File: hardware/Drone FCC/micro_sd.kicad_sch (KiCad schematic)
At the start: 15 parts, among them J701 DM3AT-SF-PEJM5

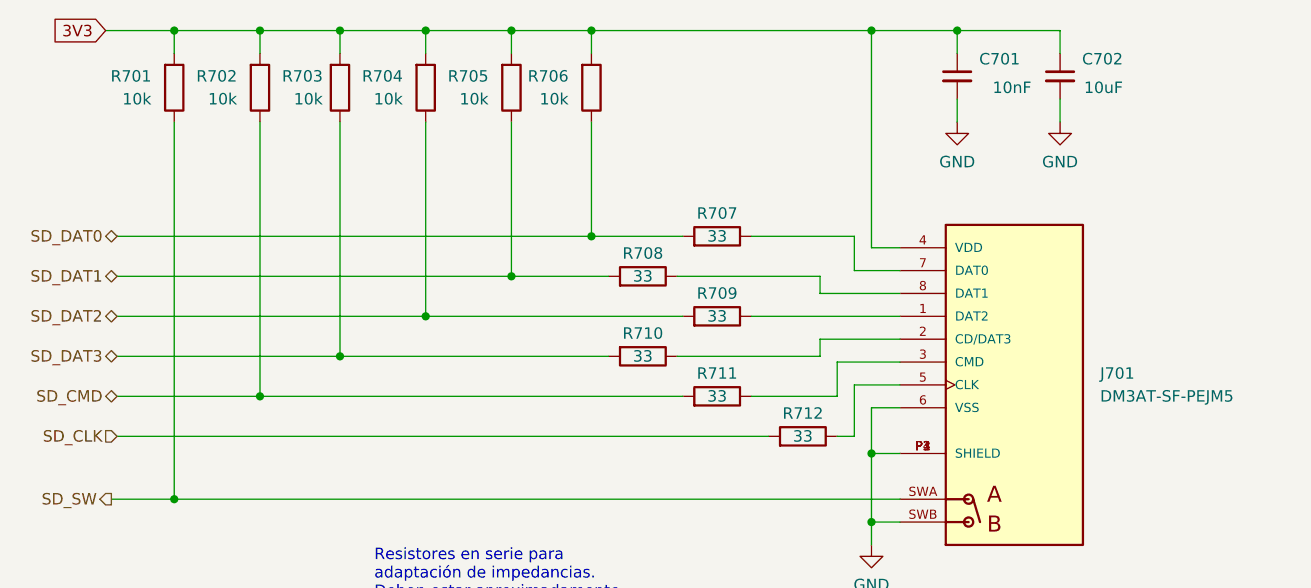
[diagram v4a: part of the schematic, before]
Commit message: re enumeation of componentes
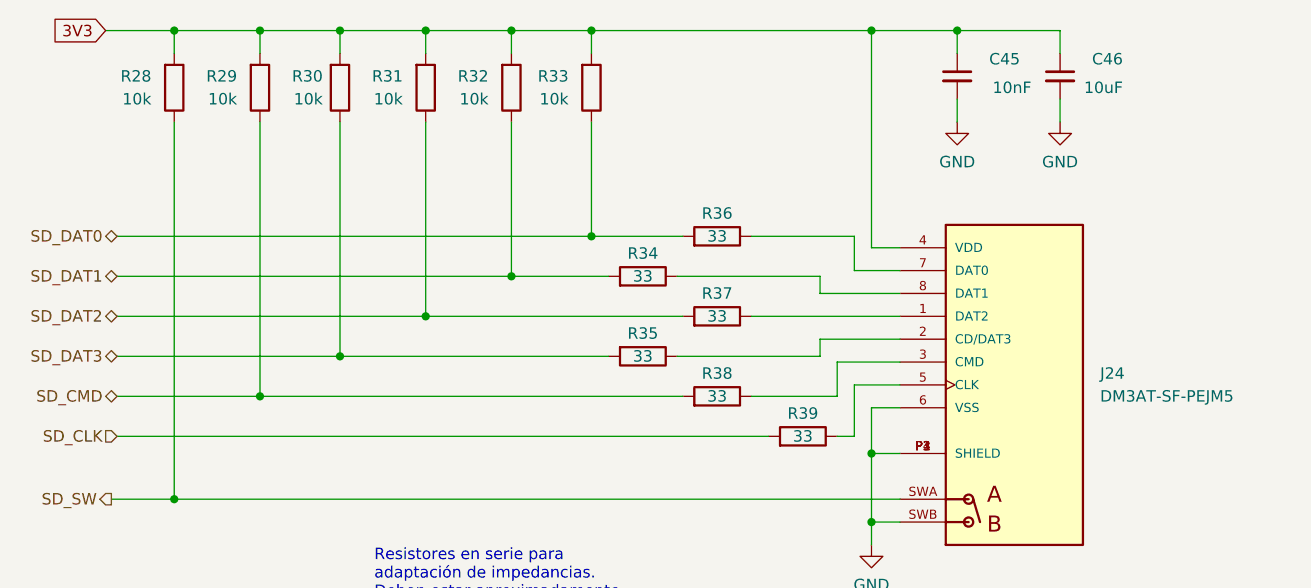
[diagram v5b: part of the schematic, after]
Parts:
- renumbered C701 to C45, C702 to C46, J701 to J24, R701 to R28, R702 to R29, R703 to R30, R704 to R31, R705 to R32, R706 to R33, R708 to R34, R710 to R35, R707 to R36, R709 to R37, R711 to R38, R712 to R39
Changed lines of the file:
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@@
   (symbol (lib_id "power:GND") (at 155.575 129.54 0) (unit 1)
     (in_bom yes) (on_board yes) (fields_autoplaced)
-    (property "Reference" "#PWR0144" (id 0) (at 155.575 135.89 0)
+    (property "Reference" "#PWR055" (id 0) (at 155.575 135.89 0)
       (effects (font (size 1.27 1.27)) hide)
     )
@@
   (symbol (lib_id "power:GND") (at 165.1 82.55 0) (unit 1)
     (in_bom yes) (on_board yes) (fields_autoplaced)
-    (property "Reference" "#PWR0142" (id 0) (at 165.1 88.9 0)
+    (property "Reference" "#PWR056" (id 0) (at 165.1 88.9 0)
       (effects (font (size 1.27 1.27)) hide)
     )
@@
   (symbol (lib_id "Device:R") (at 138.43 95.25 270) (mirror x) (unit 1)
     (in_bom yes) (on_board yes)
-    (property "Reference" "R707" (id 0) (at 138.43 92.71 90))
+    (property "Reference" "R36" (id 0) (at 138.43 92.71 90))
     (property "Value" "33" (id 1) (at 138.43 95.25 90))
     (property "Footprint" "Resistor_SMD:R_0402_1005Metric_Pad0.72x0.64mm_HandSolder" (id 2) (at 138.43 97.028 90)
@@
   (symbol (lib_id "Device:C_Small") (at 165.1 77.47 0) (unit 1)
     (in_bom yes) (on_board yes)
-    (property "Reference" "C701" (id 0) (at 172.085 75.565 0)
+    (property "Reference" "C45" (id 0) (at 172.085 75.565 0)
       (effects (font (size 1.27 1.27)) (justify right))
     )
@@
   (symbol (lib_id "DM3AT-SF-PEJM5:DM3AT-SF-PEJM5") (at 171.45 111.76 0) (unit 1)
     (in_bom yes) (on_board yes) (fields_autoplaced)
-    (property "Reference" "J701" (id 0) (at 180.975 110.4899 0)
+    (property "Reference" "J24" (id 0) (at 180.975 110.4899 0)
       (effects (font (size 1.27 1.27)) (justify left))
     )
@@
   (symbol (lib_id "Device:R") (at 106.045 78.74 0) (mirror x) (unit 1)
     (in_bom yes) (on_board yes) (fields_autoplaced)
-    (property "Reference" "R704" (id 0) (at 103.505 77.4699 0)
+    (property "Reference" "R31" (id 0) (at 103.505 77.4699 0)
       (effects (font (size 1.27 1.27)) (justify right))
     )
@@
   (symbol (lib_id "Device:R") (at 138.43 113.03 270) (mirror x) (unit 1)
     (in_bom yes) (on_board yes)
-    (property "Reference" "R711" (id 0) (at 138.43 110.49 90))
+    (property "Reference" "R38" (id 0) (at 138.43 110.49 90))
     (property "Value" "33" (id 1) (at 138.43 113.03 90))
     (property "Footprint" "Resistor_SMD:R_0402_1005Metric_Pad0.72x0.64mm_HandSolder" (id 2) (at 138.43 114.808 90)
@@
   (symbol (lib_id "Device:R") (at 115.57 78.74 0) (mirror x) (unit 1)
     (in_bom yes) (on_board yes) (fields_autoplaced)
-    (property "Reference" "R705" (id 0) (at 113.03 77.4699 0)
+    (property "Reference" "R32" (id 0) (at 113.03 77.4699 0)
       (effects (font (size 1.27 1.27)) (justify right))
     )
@@
   (symbol (lib_id "power:GND") (at 176.53 82.55 0) (unit 1)
     (in_bom yes) (on_board yes) (fields_autoplaced)
-    (property "Reference" "#PWR0143" (id 0) (at 176.53 88.9 0)
+    (property "Reference" "#PWR057" (id 0) (at 176.53 88.9 0)
       (effects (font (size 1.27 1.27)) hide)
     )
@@
   (symbol (lib_id "Device:R") (at 138.43 104.14 270) (mirror x) (unit 1)
     (in_bom yes) (on_board yes)
-    (property "Reference" "R709" (id 0) (at 138.43 101.6 90))
+    (property "Reference" "R37" (id 0) (at 138.43 101.6 90))
     (property "Value" "33" (id 1) (at 138.43 104.14 90))
     (property "Footprint" "Resistor_SMD:R_0402_1005Metric_Pad0.72x0.64mm_HandSolder" (id 2) (at 138.43 105.918 90)
@@
   (symbol (lib_id "Device:R") (at 130.175 108.585 270) (unit 1)
     (in_bom yes) (on_board yes)
-    (property "Reference" "R710" (id 0) (at 130.175 106.045 90))
+    (property "Reference" "R35" (id 0) (at 130.175 106.045 90))
     (property "Value" "33" (id 1) (at 130.175 108.585 90))
     (property "Footprint" "Resistor_SMD:R_0402_1005Metric_Pad0.72x0.64mm_HandSolder" (id 2) (at 130.175 106.807 90)
@@
   (symbol (lib_id "Device:R") (at 96.52 78.74 0) (mirror x) (unit 1)
     (in_bom yes) (on_board yes) (fields_autoplaced)
-    (property "Reference" "R703" (id 0) (at 94.615 77.4699 0)
+    (property "Reference" "R30" (id 0) (at 94.615 77.4699 0)
       (effects (font (size 1.27 1.27)) (justify right))
     )
@@
   (symbol (lib_id "Device:R") (at 78.105 78.74 0) (mirror x) (unit 1)
     (in_bom yes) (on_board yes) (fields_autoplaced)
-    (property "Reference" "R701" (id 0) (at 75.565 77.4699 0)
+    (property "Reference" "R28" (id 0) (at 75.565 77.4699 0)
       (effects (font (size 1.27 1.27)) (justify right))
     )
@@
   (symbol (lib_id "Device:R") (at 130.175 99.695 270) (mirror x) (unit 1)
     (in_bom yes) (on_board yes)
-    (property "Reference" "R708" (id 0) (at 130.175 97.155 90))
+    (property "Reference" "R34" (id 0) (at 130.175 97.155 90))
     (property "Value" "33" (id 1) (at 130.175 99.695 90))
     (property "Footprint" "Resistor_SMD:R_0402_1005Metric_Pad0.72x0.64mm_HandSolder" (id 2) (at 130.175 101.473 90)
@@
   (symbol (lib_id "Device:R") (at 87.63 78.74 0) (mirror x) (unit 1)
     (in_bom yes) (on_board yes) (fields_autoplaced)
-    (property "Reference" "R702" (id 0) (at 85.09 77.4699 0)
+    (property "Reference" "R29" (id 0) (at 85.09 77.4699 0)
       (effects (font (size 1.27 1.27)) (justify right))
     )
@@
   (symbol (lib_id "Device:R") (at 147.955 117.475 270) (mirror x) (unit 1)
     (in_bom yes) (on_board yes)
-    (property "Reference" "R712" (id 0) (at 147.955 114.935 90))
+    (property "Reference" "R39" (id 0) (at 147.955 114.935 90))
     (property "Value" "33" (id 1) (at 147.955 117.475 90))
     (property "Footprint" "Resistor_SMD:R_0402_1005Metric_Pad0.72x0.64mm_HandSolder" (id 2) (at 147.955 119.253 90)
@@
   (symbol (lib_id "Device:C_Small") (at 176.53 77.47 0) (unit 1)
     (in_bom yes) (on_board yes)
-    (property "Reference" "C702" (id 0) (at 183.515 75.565 0)
+    (property "Reference" "C46" (id 0) (at 183.515 75.565 0)
       (effects (font (size 1.27 1.27)) (justify right))
     )
@@
   (symbol (lib_id "Device:R") (at 124.46 78.74 0) (mirror x) (unit 1)
     (in_bom yes) (on_board yes) (fields_autoplaced)
-    (property "Reference" "R706" (id 0) (at 121.92 77.4699 0)
-      (effects (font (size 1.27 1.27)) (justify right))
-    )
+    (property "Reference" "R33" (id 0) (at 121.92 77.4699 0)
+      (effects (font (size 1.27 1.27)) (justify right))
+    )

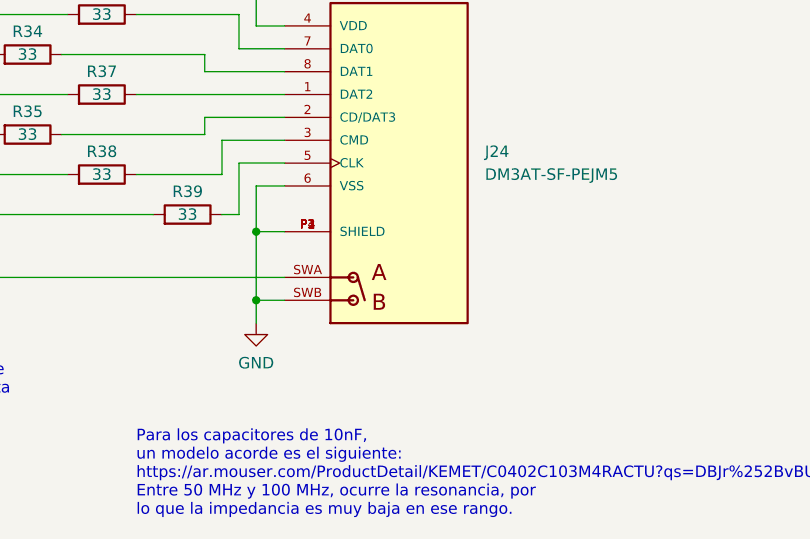
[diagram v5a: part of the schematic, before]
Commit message: moved NRST cap near mcu pin, changed v meas adc pin
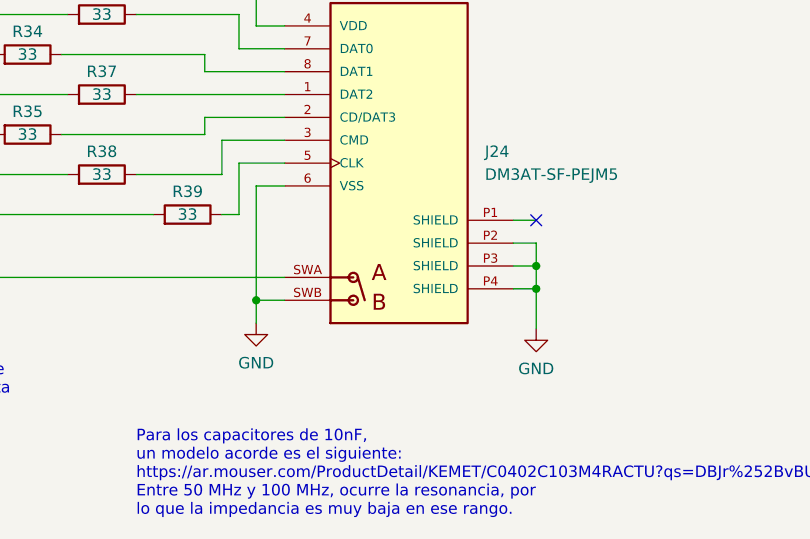
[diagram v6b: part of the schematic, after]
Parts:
- J24: footprint DM3AT-SF-PEJM5:HRS_DM3AT-SF-PEJM5 -> HRS_DM3AT-SF-PEJM5
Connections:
- net GND: no longer J24.P1 (SHIELD)
- no-connect marks 0 -> 1
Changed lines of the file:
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@@
 (kicad_sch (version 20211123) (generator eeschema)
   (paper "A4")
-  (junction (at 155.575 119.38) (diameter 0) (color 0 0 0 0)
-  )
   (junction (at 96.52 108.585) (diameter 0) (color 0 0 0 0)
   )
@@
   (junction (at 87.63 113.03) (diameter 0) (color 0 0 0 0)
   )
+  (junction (at 186.69 123.19) (diameter 0) (color 0 0 0 0)
+  )
   (junction (at 96.52 72.39) (diameter 0) (color 0 0 0 0)
   )
@@
   (junction (at 155.575 72.39) (diameter 0) (color 0 0 0 0)
   )
+  (junction (at 186.69 125.73) (diameter 0) (color 0 0 0 0)
+  )
   (junction (at 124.46 72.39) (diameter 0) (color 0 0 0 0)
   )
@@
   (junction (at 78.105 72.39) (diameter 0) (color 0 0 0 0)
   )
+  (no_connect (at 186.69 118.11))
+  (wire (pts (xy 186.69 120.65) (xy 186.69 123.19))
+    (stroke (width 0) (type default) (color 0 0 0 0))
+  )
   (wire (pts (xy 124.46 72.39) (xy 155.575 72.39))
     (stroke (width 0) (type default) (color 0 0 0 0))
@@
     (stroke (width 0) (type default) (color 0 0 0 0))
   )
+  (wire (pts (xy 186.69 123.19) (xy 186.69 125.73))
+    (stroke (width 0) (type default) (color 0 0 0 0))
+  )
   (wire (pts (xy 153.67 95.25) (xy 153.67 99.06))
     (stroke (width 0) (type default) (color 0 0 0 0))
@@
     (stroke (width 0) (type default) (color 0 0 0 0))
   )
+  (wire (pts (xy 184.15 120.65) (xy 186.69 120.65))
+    (stroke (width 0) (type default) (color 0 0 0 0))
+  )
   (wire (pts (xy 151.765 109.22) (xy 151.765 113.03))
     (stroke (width 0) (type default) (color 0 0 0 0))
@@
     (stroke (width 0) (type default) (color 0 0 0 0))
   )
+  (wire (pts (xy 186.69 125.73) (xy 186.69 130.175))
+    (stroke (width 0) (type default) (color 0 0 0 0))
+  )
   (wire (pts (xy 124.46 82.55) (xy 124.46 95.25))
     (stroke (width 0) (type default) (color 0 0 0 0))
@@
     (stroke (width 0) (type default) (color 0 0 0 0))
   )
-  (wire (pts (xy 155.575 119.38) (xy 158.75 119.38))
-    (stroke (width 0) (type default) (color 0 0 0 0))
-  )
   (wire (pts (xy 133.985 108.585) (xy 149.86 108.585))
     (stroke (width 0) (type default) (color 0 0 0 0))
   )
+  (wire (pts (xy 184.15 123.19) (xy 186.69 123.19))
+    (stroke (width 0) (type default) (color 0 0 0 0))
+  )
   (wire (pts (xy 158.75 99.06) (xy 153.67 99.06))
     (stroke (width 0) (type default) (color 0 0 0 0))
   )
+  (wire (pts (xy 184.15 118.11) (xy 186.69 118.11))
+    (stroke (width 0) (type default) (color 0 0 0 0))
+  )
   (wire (pts (xy 71.755 104.14) (xy 106.045 104.14))
     (stroke (width 0) (type default) (color 0 0 0 0))
@@
     (stroke (width 0) (type default) (color 0 0 0 0))
   )
-  (wire (pts (xy 155.575 119.38) (xy 155.575 127))
-    (stroke (width 0) (type default) (color 0 0 0 0))
-  )
   (wire (pts (xy 96.52 72.39) (xy 96.52 74.93))
     (stroke (width 0) (type default) (color 0 0 0 0))
@@
     (stroke (width 0) (type default) (color 0 0 0 0))
   )
-  (wire (pts (xy 155.575 114.3) (xy 155.575 119.38))
+  (wire (pts (xy 155.575 114.3) (xy 155.575 127))
+    (stroke (width 0) (type default) (color 0 0 0 0))
+  )
+  (wire (pts (xy 184.15 125.73) (xy 186.69 125.73))
     (stroke (width 0) (type default) (color 0 0 0 0))
   )
@@
       (effects (font (size 1.27 1.27)) (justify left))
     )
-    (property "Footprint" "DM3AT-SF-PEJM5:HRS_DM3AT-SF-PEJM5" (id 2) (at 171.45 111.76 0)
+    (property "Footprint" "HRS_DM3AT-SF-PEJM5" (id 2) (at 171.45 111.76 0)
       (effects (font (size 1.27 1.27)) (justify bottom) hide)
     )
@@
     (pin "2")
   )
+  (symbol (lib_id "power:GND") (at 186.69 130.175 0) (unit 1)
+    (in_bom yes) (on_board yes) (fields_autoplaced)
+    (property "Reference" "#PWR0103" (id 0) (at 186.69 136.525 0)
+      (effects (font (size 1.27 1.27)) hide)
+    )
+    (property "Value" "GND" (id 1) (at 186.69 134.62 0))
+    (property "Footprint" "" (id 2) (at 186.69 130.175 0)
+      (effects (font (size 1.27 1.27)) hide)
+    )
+    (property "Datasheet" "" (id 3) (at 186.69 130.175 0)
+      (effects (font (size 1.27 1.27)) hide)
+    )
+    (pin "1")
+  )
   (symbol (lib_id "Device:R") (at 78.105 78.74 0) (mirror x) (unit 1)
